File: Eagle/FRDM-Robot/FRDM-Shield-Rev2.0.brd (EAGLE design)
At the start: 72.1 x 56.6 mm, 7 parts

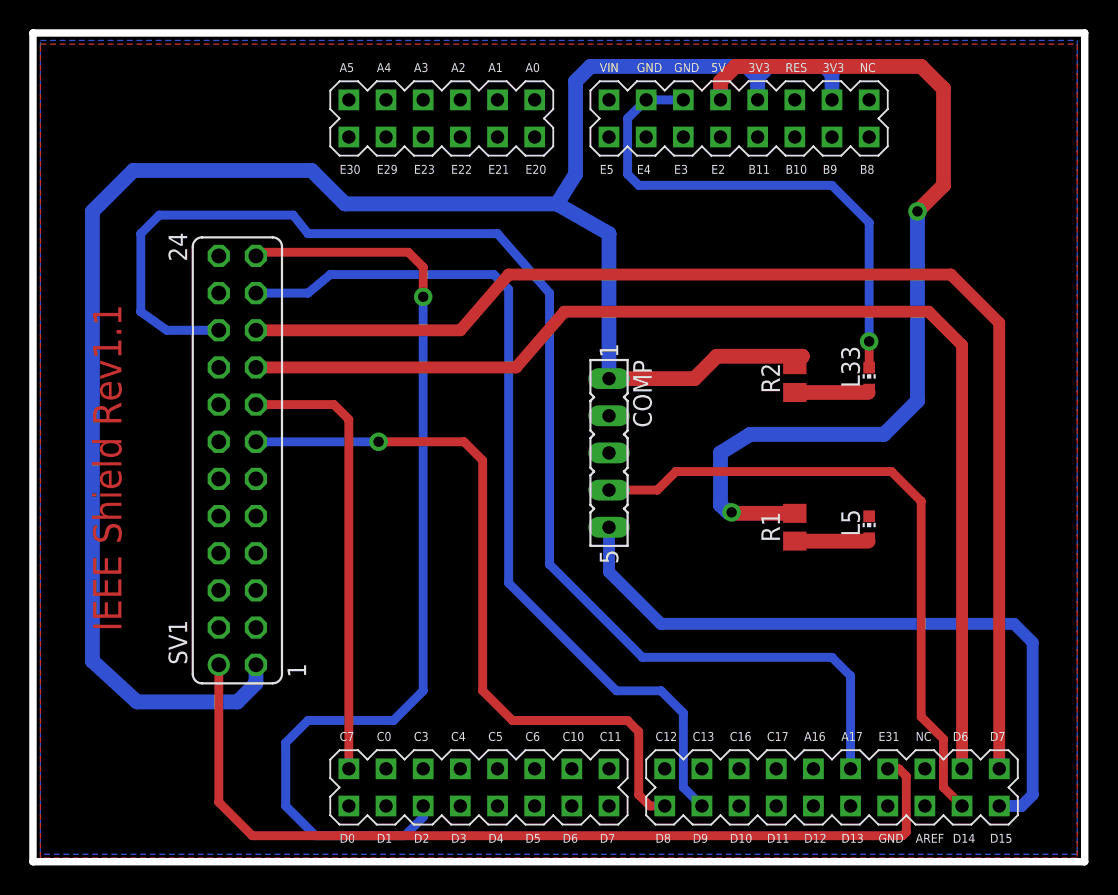
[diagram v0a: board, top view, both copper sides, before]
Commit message: updated FRDM-Shield 2.0 revision
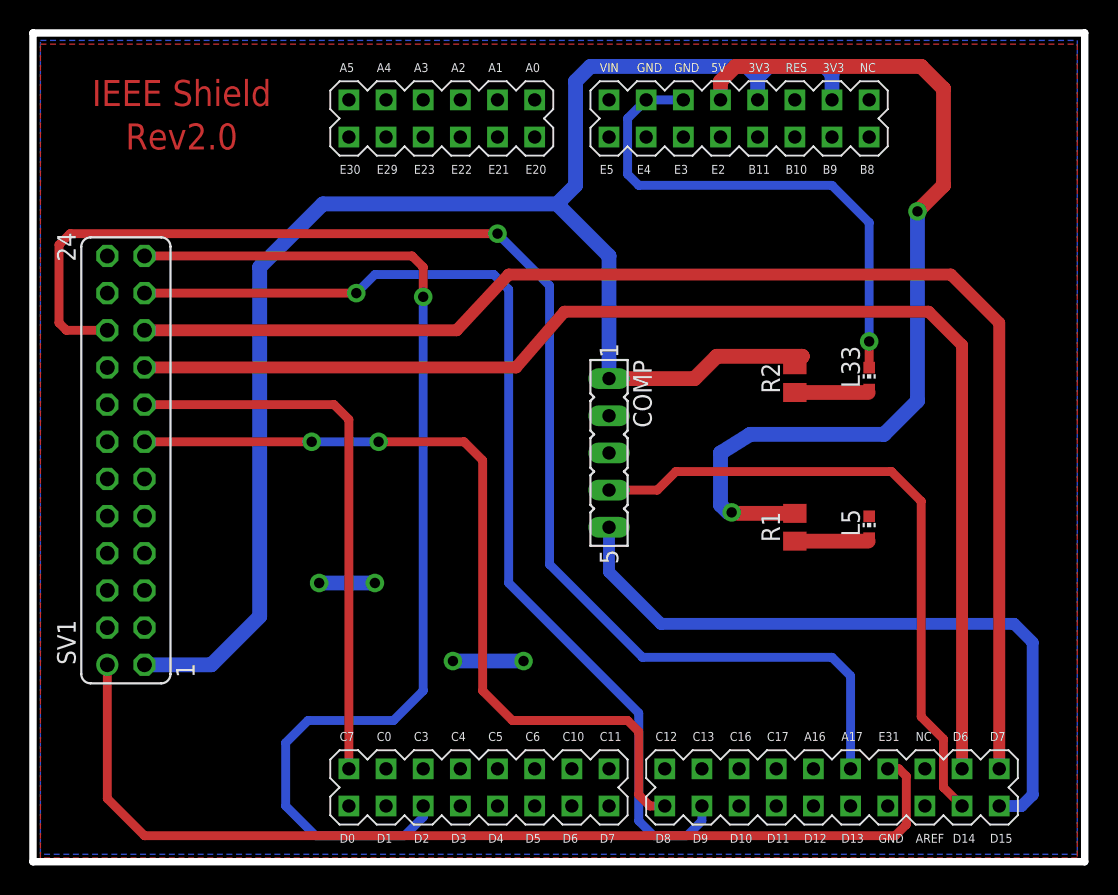
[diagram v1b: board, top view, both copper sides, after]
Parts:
- moved SV1 7.62 mm to (6.35, 27.4)
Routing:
- net +3V3: track 138.1 -> 114.3 mm
- net SPICLK: track 60.7 -> 72.0 mm, vias 0 -> 1
- net GND: track 35.9 -> 44.6 mm, vias 1 -> 5
- net MOSI: track 79.9 -> 87.5 mm
- net ATTN: track 30.6 -> 38.3 mm
- net RESET: track 50.0 -> 57.6 mm, vias 1 -> 2
- net MISO: track 84.4 -> 91.9 mm
- net SS: track 67.6 -> 75.0 mm
- net IRQ: track 62.7 -> 69.9 mm
- net RXTXEN: track 90.6 -> 93.3 mm, vias 0 -> 1
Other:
- board text added: "IEEE Shield Rev2.0"
- board text removed: "IEEE Shield Rev1.1"
